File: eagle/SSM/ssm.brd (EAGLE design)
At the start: 71.1 x 38.7 mm, 21 parts, among them IC1 4051N, IC2 MCP604P

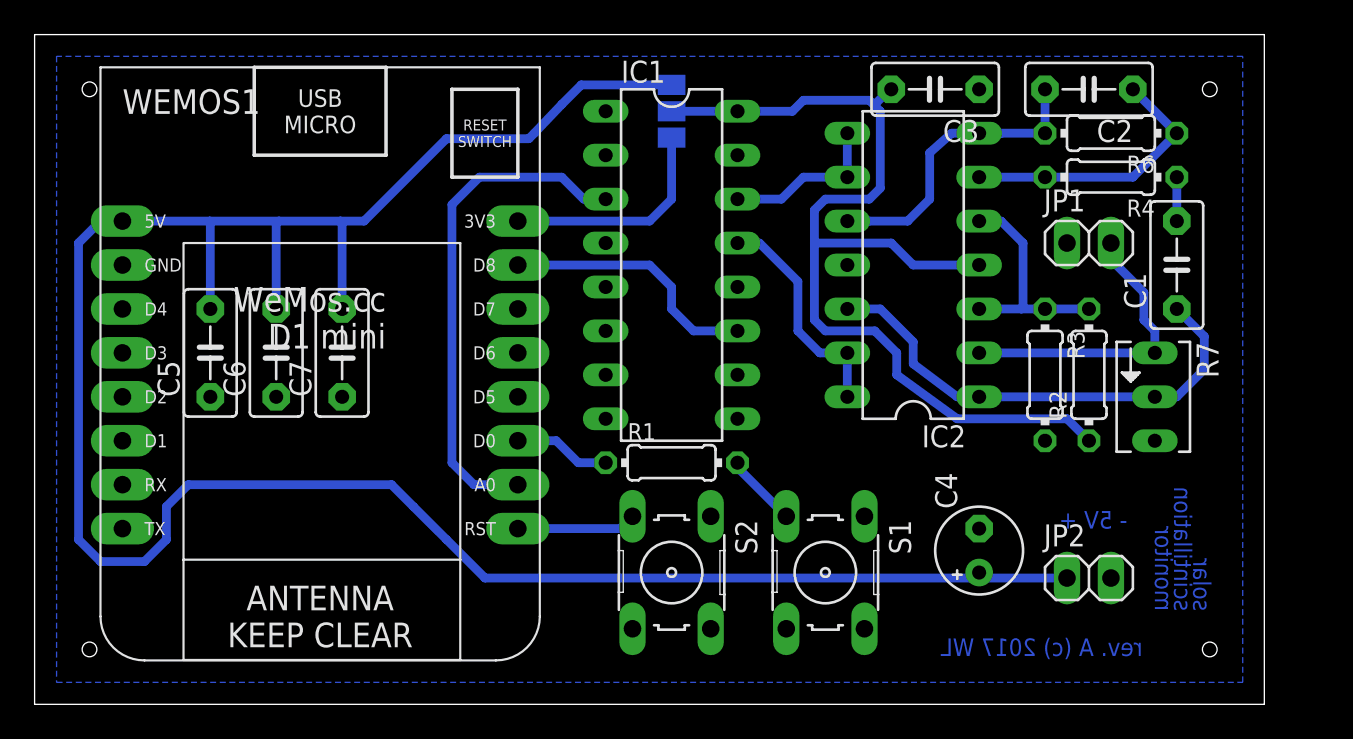
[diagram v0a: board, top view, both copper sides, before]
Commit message: realign board for ordered parts
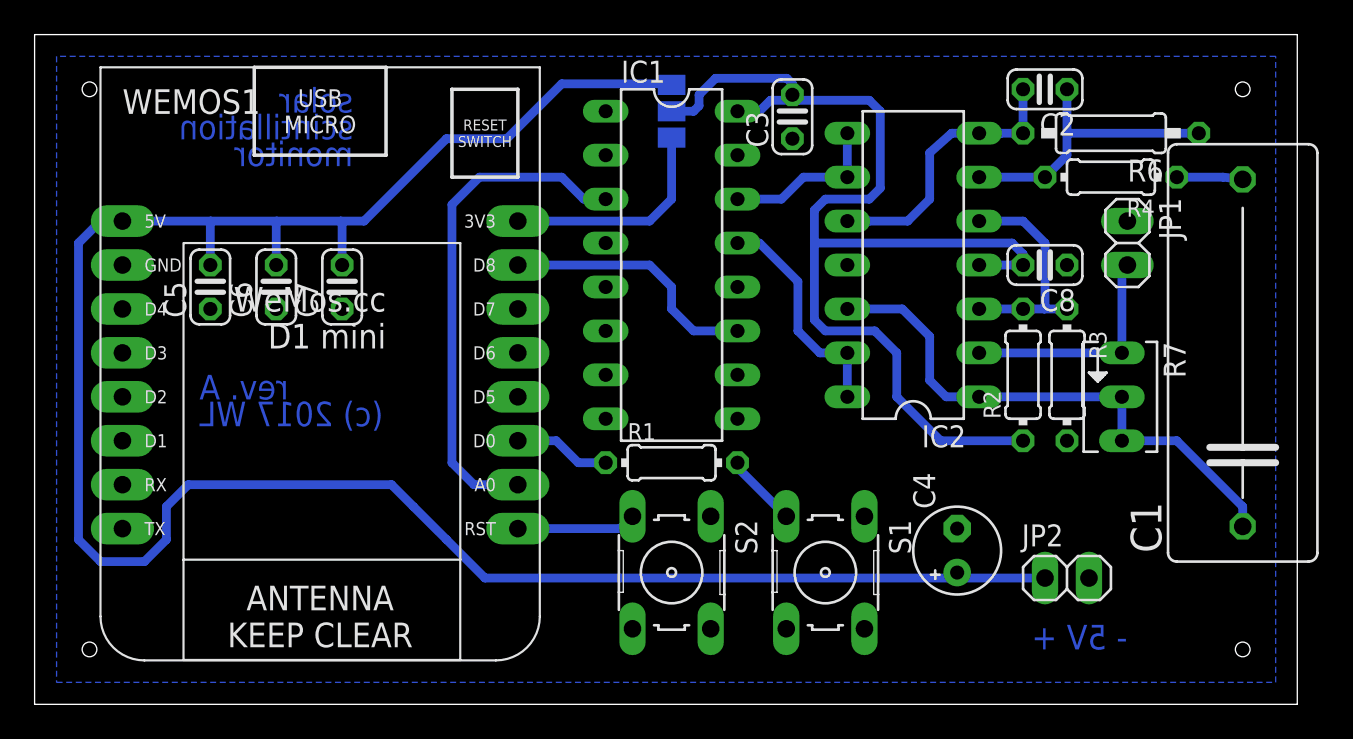
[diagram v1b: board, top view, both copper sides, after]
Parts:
- added C8: 120p, rcl:C025-024X044
- C1: device capacitor-wima:C5B3 -> Cap:C225-087X210
- C2, C3, C5, C6, C7: device capacitor-wima:C5B3 -> rcl:C025-024X044
- R6: device resistor:0204/7 -> rcl:0207/10
- moved C3 8.41 mm to (74.3, 59.4), turned to 90 degrees
- moved C1 5.39 mm to (100.3, 47.0)
- moved C5 3.81 mm to (40.6, 49.5)
- moved C6 3.81 mm to (44.5, 49.5)
- moved C7 3.81 mm to (48.3, 49.5)
- moved R2 3.81 mm to (87.6, 44.5)
- moved C2 2.54 mm to (88.9, 61.0)
- moved JP1 2.22 mm to (93.7, 52.1), turned to 270 degrees
- moved R7 1.91 mm to (93.3, 43.2)
- moved C4 1.27 mm to (83.8, 34.3)
- moved JP2 1.27 mm to (90.2, 32.7)
- moved R3 1.27 mm to (90.2, 44.5)
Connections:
- net GND: now also C8.1
- net N$5: now also R7.A
- net VCC: now also C8.2
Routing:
- net +5V: track 133.8 -> 124.9 mm
- net VCC: track 58.4 -> 65.1 mm
- net N$2: track 17.6 -> 13.8 mm
- net N$5: track 28.1 -> 31.7 mm
- net N$6: track 2.54 -> 3.82 mm
- net N$8: track 20.1 -> 18.9 mm
- net N$7: track 16.1 -> 17.1 mm
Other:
- board size 71.1 x 38.7 mm -> 73 x 38.7 mm
